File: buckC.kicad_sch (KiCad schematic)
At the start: 34 parts, among them Q1 SSM3K15AMFV,L3F, U1 SiC437BED-T1-GE3

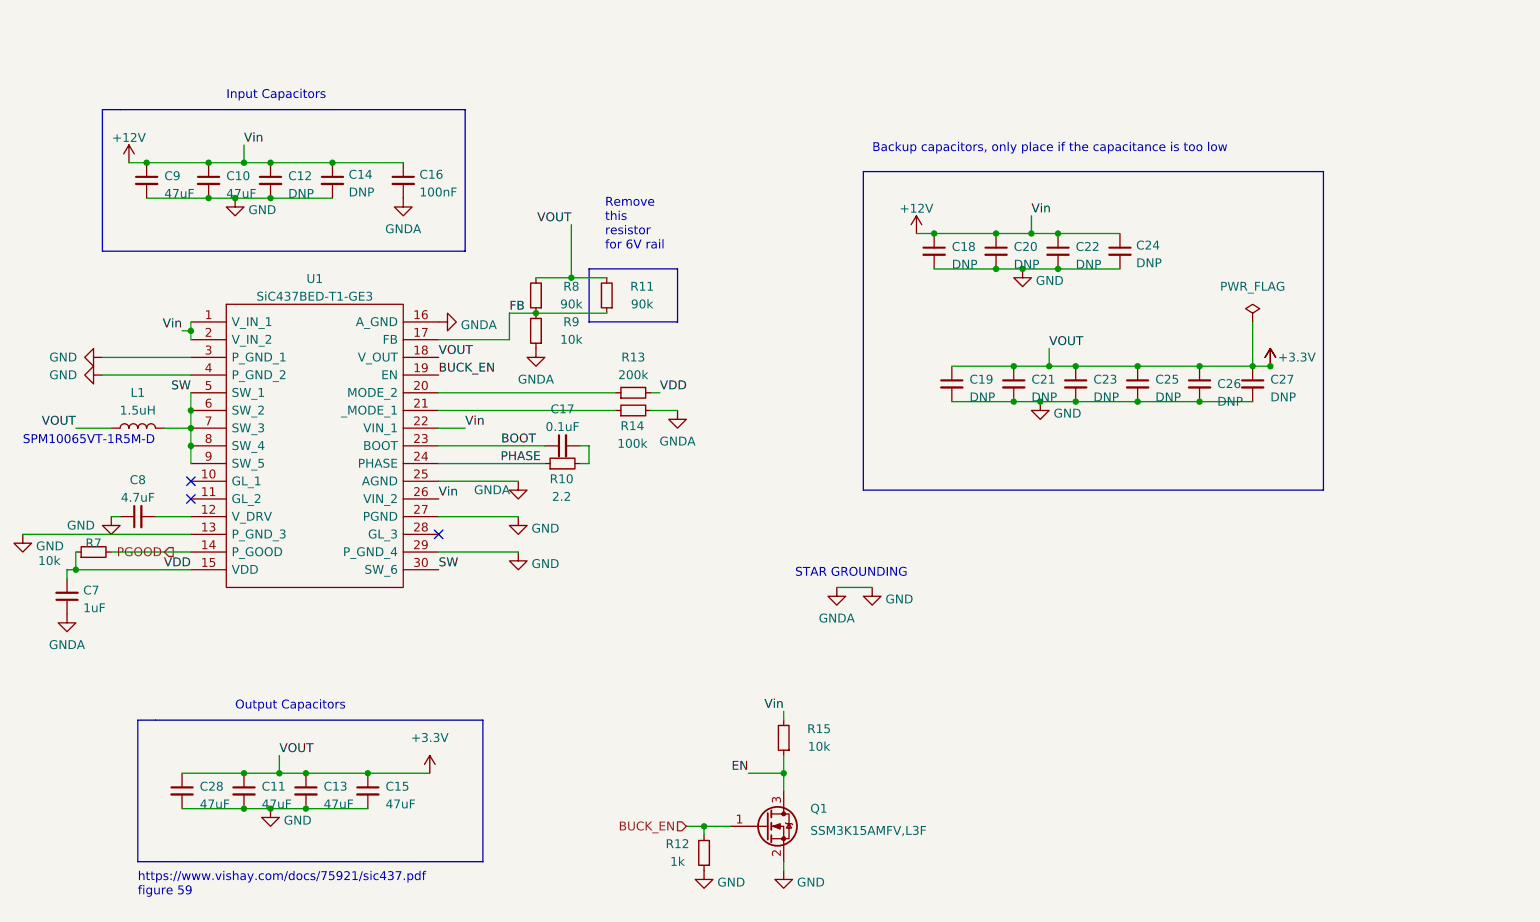
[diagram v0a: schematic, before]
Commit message: Overhaul of design
Changed out the SFMC Oresat connectors for the 46010-0622 Molex; added the SC4215; reduced from 4 connectors to three connectors - no changes made to the footprint, changes only made to the schematic for checks
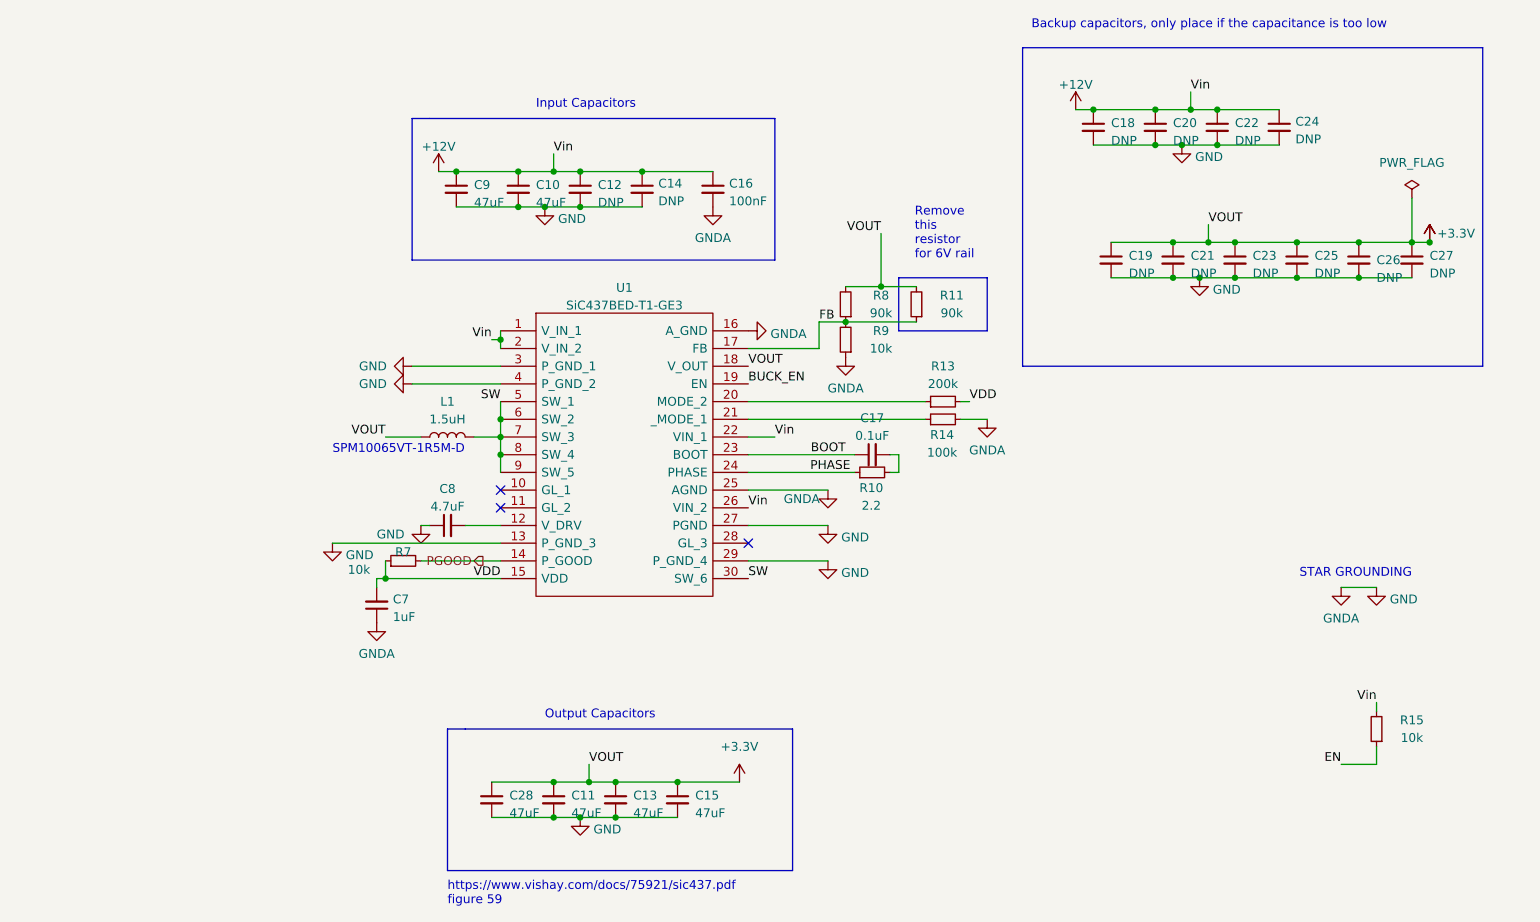
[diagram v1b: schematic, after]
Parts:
- removed Q1: SSM3K15AMFV,L3F, Package_TO_SOT_SMD:SOT-723, symbol Device:Q_NMOS_GSD
- removed R12: 1k, Resistor_SMD:R_0402_1005Metric, symbol Device:R_Small
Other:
- moved on the sheet: C10, C11, C12, C13, C14, C15, C16, C17, C18, C19, C20, C21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
